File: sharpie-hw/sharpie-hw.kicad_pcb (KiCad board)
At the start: 2 copper layers, 62.8 x 38.8 mm, 62 parts, among them J2 Conn_01x02_MountingPin, J3 Conn_01x03_MountingPin, J4 Conn_01x08, J5 Conn_01x14, J6 LS021B7DD02, SW1 SW_Push_Cross, SW2 SW_Push_Cross, U1 TPS7A2533, U2 TPS7A2501, U3 RP2350_60QFN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

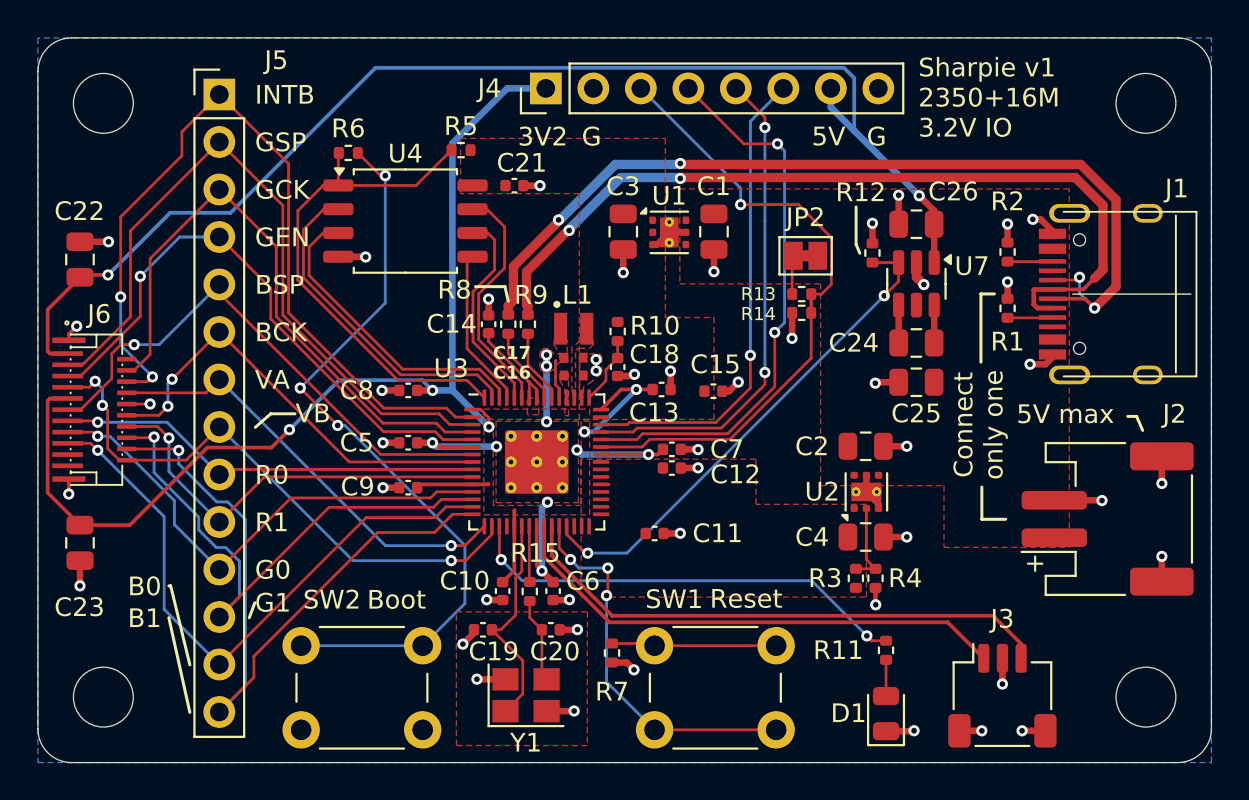
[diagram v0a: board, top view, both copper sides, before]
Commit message: PCB changes of some kind: appears to be the version sent to JLC.
The manufactured version of the PCB has no voltage divider or battery input,
because they were unnecssary (and in the case of the battery input,
unsafe).
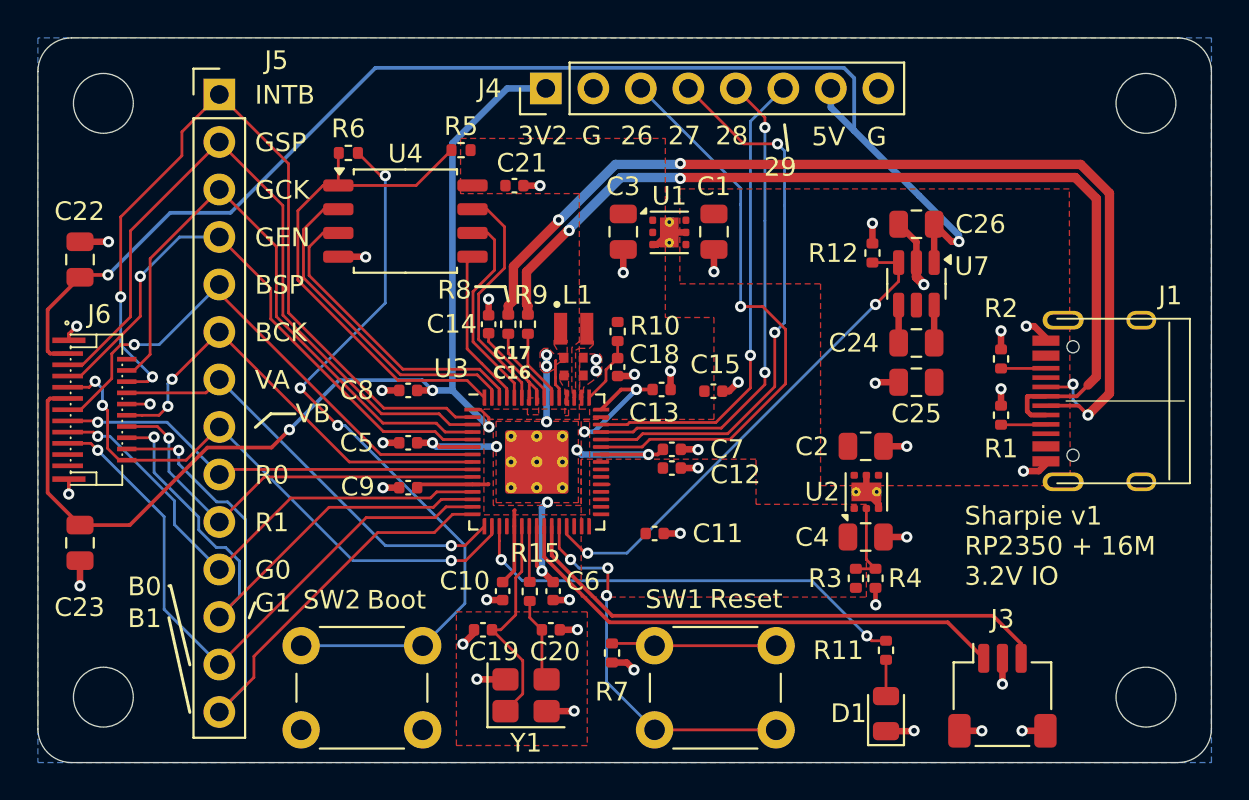
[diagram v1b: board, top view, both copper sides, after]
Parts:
- removed J2: Conn_01x02_MountingPin, Connector_JST:JST_PH_S2B-PH-SM4-TB_1x02-1MP_P2.00mm_Horizontal
- removed JP2: BatteryVoltageJumper, Jumper:SolderJumper-2_P1.3mm_Bridged_Pad1.0x1.5mm
- removed R13: 33k, Resistor_SMD:R_0402_1005Metric
- removed R14: 47k, Resistor_SMD:R_0402_1005Metric
- moved J1 5.73 mm to (79.4, 42.9)
- moved R2 5.73 mm to (71.9, 40.6)
- moved R1 5.73 mm to (71.9, 43.6)
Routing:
- net GND: track 57.3 -> 51.5 mm, vias 47 -> 42
- net D+: track 49.9 -> 55.5 mm
- net D-: track 46.7 -> 52.3 mm
- net /MCU/EX_B4: track 34.4 -> 31.0 mm
- net +5V: track 67.6 -> 70.8 mm
- net Net-(JP2-B): track 2.18 -> 0.00 mm
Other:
- board text added: "26"
- board text added: "27"
- board text added: "28"
- board text added: "29"
- board text added: "Sharpie v1 RP2350 + 16M 3.2V IO"
- board text removed: "+"
- board text removed: "5V max"
- board text removed: "Connect only one"
- board text removed: "Sharpie v1 2350+16M 3.2V IO"
